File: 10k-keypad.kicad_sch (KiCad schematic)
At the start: 62 parts, among them J1 AVR-ISP-6, K1 SW_Push, K10 SW_Push, K2 SW_Push, K3 SW_Push, K4 SW_Push, K5 SW_Push, K6 SW_Push, K7 SW_Push, K8 SW_Push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

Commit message: fix schematic, gerbers
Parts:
- C16, C17, C18, C8: value 0.1u -> 100n
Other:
- note added: "ATMEGA32U4"
- note removed: "ATMEGA16U2"
- moved on the sheet: C10, C11, C12, C13, C14, C15, C5, C6, C7, C9, D12, D13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

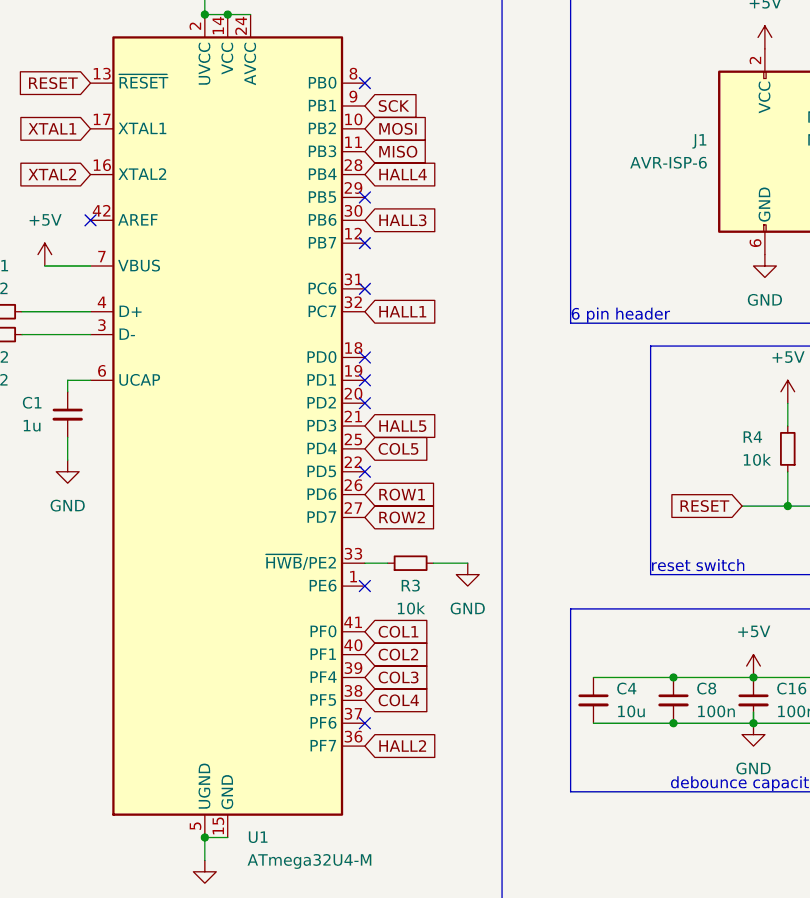
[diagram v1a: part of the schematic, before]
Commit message: redo all routing, remove unused footprint
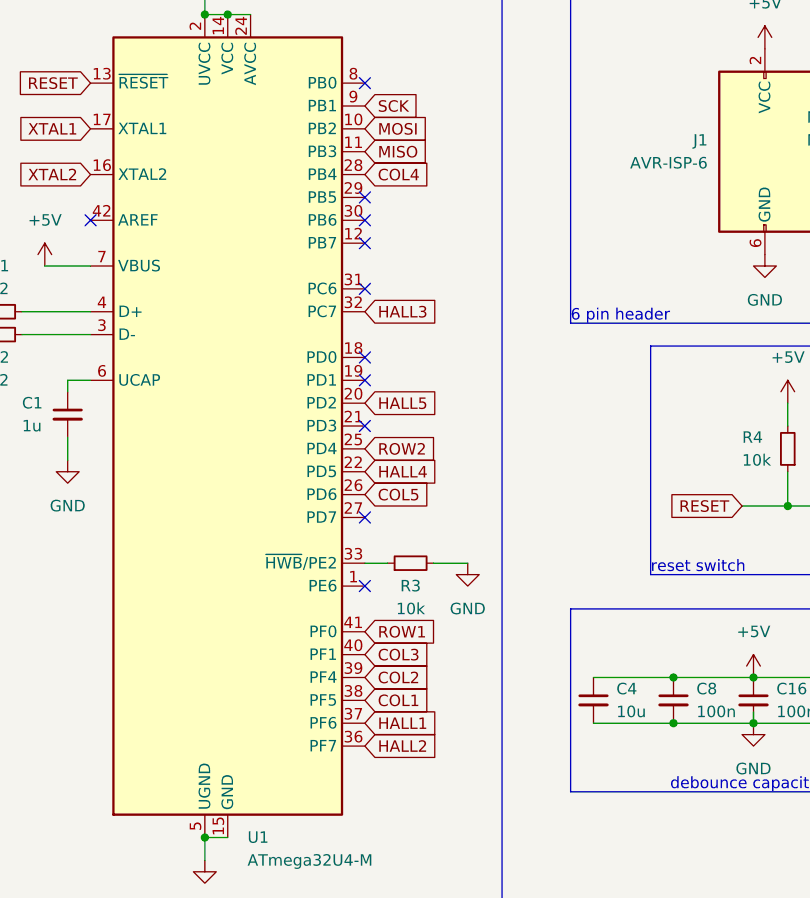
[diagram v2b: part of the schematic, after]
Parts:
- K10, K6, K7, K8, K9: footprint Hall:SW_MX_HS_CPG151101S11_1u_no_center_piece -> marbastlib-mx:SW_MX_HS_CPG151101S11_1u
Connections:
- net COL1: now also U1.38 (PF5); no longer U1.41 (PF0)
- net COL2: now also U1.39 (PF4); no longer U1.40 (PF1)
- net COL3: now also U1.40 (PF1); no longer U1.39 (PF4)
- net COL4: now also U1.28 (PB4); no longer U1.38 (PF5)
- net COL5: now also U1.26 (PD6); no longer U1.25 (PD4)
- net HALL1: now also U1.37 (PF6); no longer U1.32 (PC7)
- net HALL3: now also U1.32 (PC7); no longer U1.30 (PB6)
- net HALL4: now also U1.22 (PD5); no longer U1.28 (PB4)
- net HALL5: now also U1.20 (PD2); no longer U1.21 (PD3)
- net ROW1: now also U1.41 (PF0); no longer U1.26 (PD6)
- net ROW2: now also U1.25 (PD4); no longer U1.27 (PD7)
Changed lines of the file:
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@@
   (no_connect (at 210.82 69.85))
   (no_connect (at 210.82 102.87))
-  (no_connect (at 210.82 105.41))
+  (no_connect (at 210.82 107.95))
   (no_connect (at 38.1 175.26))
   (no_connect (at 38.1 160.02))
   (no_connect (at 210.82 92.71))
-  (no_connect (at 210.82 113.03))
-  (no_connect (at 210.82 140.97))
+  (no_connect (at 210.82 118.11))
+  (no_connect (at 210.82 85.09))
   (no_connect (at 210.82 87.63))
   (no_connect (at 180.34 85.09))
@@
     )
   )
-  (global_label "COL3" (shape input) (at 210.82 135.89 0) (fields_autoplaced)
+  (global_label "COL3" (shape input) (at 210.82 133.35 0) (fields_autoplaced)
     (effects (font (size 1.27 1.27)) (justify left))
-    (property "Intersheetrefs" "${INTERSHEET_REFS}" (at 218.6433 135.89 0)
+    (property "Intersheetrefs" "${INTERSHEET_REFS}" (at 218.6433 133.35 0)
       (effects (font (size 1.27 1.27)) (justify left) hide)
     )
@@
     )
   )
-  (global_label "COL2" (shape input) (at 210.82 133.35 0) (fields_autoplaced)
+  (global_label "COL2" (shape input) (at 210.82 135.89 0) (fields_autoplaced)
     (effects (font (size 1.27 1.27)) (justify left))
-    (property "Intersheetrefs" "${INTERSHEET_REFS}" (at 218.6433 133.35 0)
+    (property "Intersheetrefs" "${INTERSHEET_REFS}" (at 218.6433 135.89 0)
       (effects (font (size 1.27 1.27)) (justify left) hide)
     )
@@
     )
   )
-  (global_label "HALL1" (shape input) (at 210.82 95.25 0) (fields_autoplaced)
+  (global_label "HALL1" (shape input) (at 210.82 140.97 0) (fields_autoplaced)
     (effects (font (size 1.27 1.27)) (justify left))
-    (property "Intersheetrefs" "${INTERSHEET_REFS}" (at 219.49 95.25 0)
+    (property "Intersheetrefs" "${INTERSHEET_REFS}" (at 219.49 140.97 0)
       (effects (font (size 1.27 1.27)) (justify left) hide)
     )
   )
-  (global_label "ROW1" (shape input) (at 210.82 115.57 0) (fields_autoplaced)
+  (global_label "ROW1" (shape input) (at 210.82 130.81 0) (fields_autoplaced)
     (effects (font (size 1.27 1.27)) (justify left))
-    (property "Intersheetrefs" "${INTERSHEET_REFS}" (at 219.0666 115.57 0)
+    (property "Intersheetrefs" "${INTERSHEET_REFS}" (at 219.0666 130.81 0)
       (effects (font (size 1.27 1.27)) (justify left) hide)
     )
@@
     )
   )
-  (global_label "COL5" (shape input) (at 210.82 110.49 0) (fields_autoplaced)
+  (global_label "COL5" (shape input) (at 210.82 115.57 0) (fields_autoplaced)
     (effects (font (size 1.27 1.27)) (justify left))
-    (property "Intersheetrefs" "${INTERSHEET_REFS}" (at 218.6433 110.49 0)
+    (property "Intersheetrefs" "${INTERSHEET_REFS}" (at 218.6433 115.57 0)
       (effects (font (size 1.27 1.27)) (justify left) hide)
     )
@@
     )
   )
-  (global_label "HALL4" (shape input) (at 210.82 80.01 0) (fields_autoplaced)
+  (global_label "HALL4" (shape input) (at 210.82 113.03 0) (fields_autoplaced)
     (effects (font (size 1.27 1.27)) (justify left))
-    (property "Intersheetrefs" "${INTERSHEET_REFS}" (at 219.49 80.01 0)
+    (property "Intersheetrefs" "${INTERSHEET_REFS}" (at 219.49 113.03 0)
       (effects (font (size 1.27 1.27)) (justify left) hide)
     )
@@
     )
   )
-  (global_label "HALL3" (shape input) (at 210.82 85.09 0) (fields_autoplaced)
+  (global_label "HALL3" (shape input) (at 210.82 95.25 0) (fields_autoplaced)
     (effects (font (size 1.27 1.27)) (justify left))
-    (property "Intersheetrefs" "${INTERSHEET_REFS}" (at 219.49 85.09 0)
+    (property "Intersheetrefs" "${INTERSHEET_REFS}" (at 219.49 95.25 0)
       (effects (font (size 1.27 1.27)) (justify left) hide)
     )
@@
     )
   )
-  (global_label "COL1" (shape input) (at 210.82 130.81 0) (fields_autoplaced)
+  (global_label "COL1" (shape input) (at 210.82 138.43 0) (fields_autoplaced)
     (effects (font (size 1.27 1.27)) (justify left))
-    (property "Intersheetrefs" "${INTERSHEET_REFS}" (at 218.6433 130.81 0)
+    (property "Intersheetrefs" "${INTERSHEET_REFS}" (at 218.6433 138.43 0)
       (effects (font (size 1.27 1.27)) (justify left) hide)
     )
@@
     )
   )
-  (global_label "COL4" (shape input) (at 210.82 138.43 0) (fields_autoplaced)
+  (global_label "COL4" (shape input) (at 210.82 80.01 0) (fields_autoplaced)
     (effects (font (size 1.27 1.27)) (justify left))
-    (property "Intersheetrefs" "${INTERSHEET_REFS}" (at 218.6433 138.43 0)
+    (property "Intersheetrefs" "${INTERSHEET_REFS}" (at 218.6433 80.01 0)
       (effects (font (size 1.27 1.27)) (justify left) hide)
     )
@@
     )
   )
-  (global_label "HALL5" (shape input) (at 210.82 107.95 0) (fields_autoplaced)
+  (global_label "HALL5" (shape input) (at 210.82 105.41 0) (fields_autoplaced)
     (effects (font (size 1.27 1.27)) (justify left))
-    (property "Intersheetrefs" "${INTERSHEET_REFS}" (at 219.49 107.95 0)
+    (property "Intersheetrefs" "${INTERSHEET_REFS}" (at 219.49 105.41 0)
       (effects (font (size 1.27 1.27)) (justify left) hide)
     )
@@
     )
   )
-  (global_label "ROW2" (shape input) (at 210.82 118.11 0) (fields_autoplaced)
+  (global_label "ROW2" (shape input) (at 210.82 110.49 0) (fields_autoplaced)
     (effects (font (size 1.27 1.27)) (justify left))
-    (property "Intersheetrefs" "${INTERSHEET_REFS}" (at 219.0666 118.11 0)
+    (property "Intersheetrefs" "${INTERSHEET_REFS}" (at 219.0666 110.49 0)
       (effects (font (size 1.27 1.27)) (justify left) hide)
     )
@@
       (effects (font (size 1.27 1.27)) hide)
     )
-    (property "Footprint" "Hall:SW_MX_HS_CPG151101S11_1u_no_center_piece" (at 96.52 123.19 0)
+    (property "Footprint" "marbastlib-mx:SW_MX_HS_CPG151101S11_1u" (at 96.52 123.19 0)
       (effects (font (size 1.27 1.27)) hide)
     )
@@
       (effects (font (size 1.27 1.27)) hide)
     )
-    (property "Footprint" "Hall:SW_MX_HS_CPG151101S11_1u_no_center_piece" (at 66.04 123.19 0)
+    (property "Footprint" "marbastlib-mx:SW_MX_HS_CPG151101S11_1u" (at 66.04 123.19 0)
       (effects (font (size 1.27 1.27)) hide)
     )
@@
       (effects (font (size 1.27 1.27)) hide)
     )
-    (property "Footprint" "Hall:SW_MX_HS_CPG151101S11_1u_no_center_piece" (at 50.8 123.19 0)
+    (property "Footprint" "marbastlib-mx:SW_MX_HS_CPG151101S11_1u" (at 50.8 123.19 0)
       (effects (font (size 1.27 1.27)) hide)
     )
@@
       (effects (font (size 1.27 1.27)) hide)
     )
-    (property "Footprint" "Hall:SW_MX_HS_CPG151101S11_1u_no_center_piece" (at 35.56 123.19 0)
+    (property "Footprint" "marbastlib-mx:SW_MX_HS_CPG151101S11_1u" (at 35.56 123.19 0)
       (effects (font (size 1.27 1.27)) hide)
     )
@@
       (effects (font (size 1.27 1.27)) hide)
     )
-    (property "Footprint" "Hall:SW_MX_HS_CPG151101S11_1u_no_center_piece" (at 81.28 123.19 0)
-      (effects (font (size 1.27 1.27)) hide)
-    )
+    (property "Footprint" "marbastlib-mx:SW_MX_HS_CPG151101S11_1u" (at 81.28 123.19 0)
+      (effects (font (size 1.27 1.27)) hide)
+    )

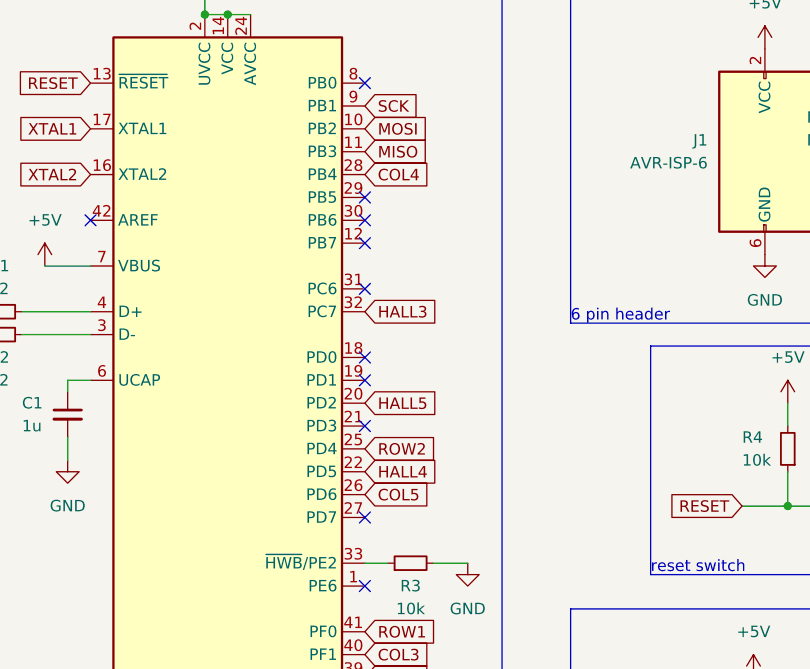
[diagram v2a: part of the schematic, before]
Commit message: correct analog pins
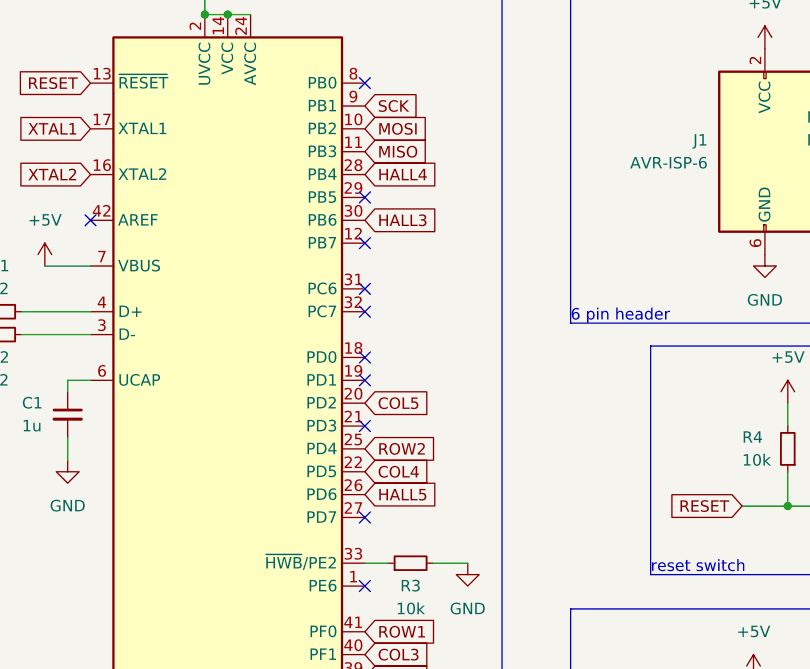
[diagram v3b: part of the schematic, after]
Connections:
- net COL4: now also U1.22 (PD5); no longer U1.28 (PB4)
- net COL5: now also U1.20 (PD2); no longer U1.26 (PD6)
- net HALL3: now also U1.30 (PB6); no longer U1.32 (PC7)
- net HALL4: now also U1.28 (PB4); no longer U1.22 (PD5)
- net HALL5: now also U1.26 (PD6); no longer U1.20 (PD2)

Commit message: move hall sensors to center
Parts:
- K10, K6, K7, K8, K9: footprint marbastlib-mx:SW_MX_HS_CPG151101S11_1u -> custom:SW_MX_HS_CPG151101S11_1u_no_center
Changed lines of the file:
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@@
 			)
 		)
-		(property "Footprint" "marbastlib-mx:SW_MX_HS_CPG151101S11_1u"
+		(property "Footprint" "custom:SW_MX_HS_CPG151101S11_1u_no_center"
 			(at 96.52 123.19 0)
 			(effects
@@
 			)
 		)
-		(property "Footprint" "marbastlib-mx:SW_MX_HS_CPG151101S11_1u"
+		(property "Footprint" "custom:SW_MX_HS_CPG151101S11_1u_no_center"
 			(at 66.04 123.19 0)
 			(effects
@@
 			)
 		)
-		(property "Footprint" "marbastlib-mx:SW_MX_HS_CPG151101S11_1u"
+		(property "Footprint" "custom:SW_MX_HS_CPG151101S11_1u_no_center"
 			(at 50.8 123.19 0)
 			(effects
@@
 			)
 		)
-		(property "Footprint" "marbastlib-mx:SW_MX_HS_CPG151101S11_1u"
+		(property "Footprint" "custom:SW_MX_HS_CPG151101S11_1u_no_center"
 			(at 35.56 123.19 0)
 			(effects
@@
 			)
 		)
-		(property "Footprint" "marbastlib-mx:SW_MX_HS_CPG151101S11_1u"
+		(property "Footprint" "custom:SW_MX_HS_CPG151101S11_1u_no_center"
 			(at 81.28 123.19 0)
 			(effects
